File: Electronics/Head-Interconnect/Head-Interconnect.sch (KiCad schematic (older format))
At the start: 26 parts, among them J2 Conn_02x03_Odd_Even, J3 Conn_Coaxial, J4 Conn_01x04_MountingPin, J5 Conn_Coaxial, J6 Conn_01x04, J7 Conn_01x20_MountingPin

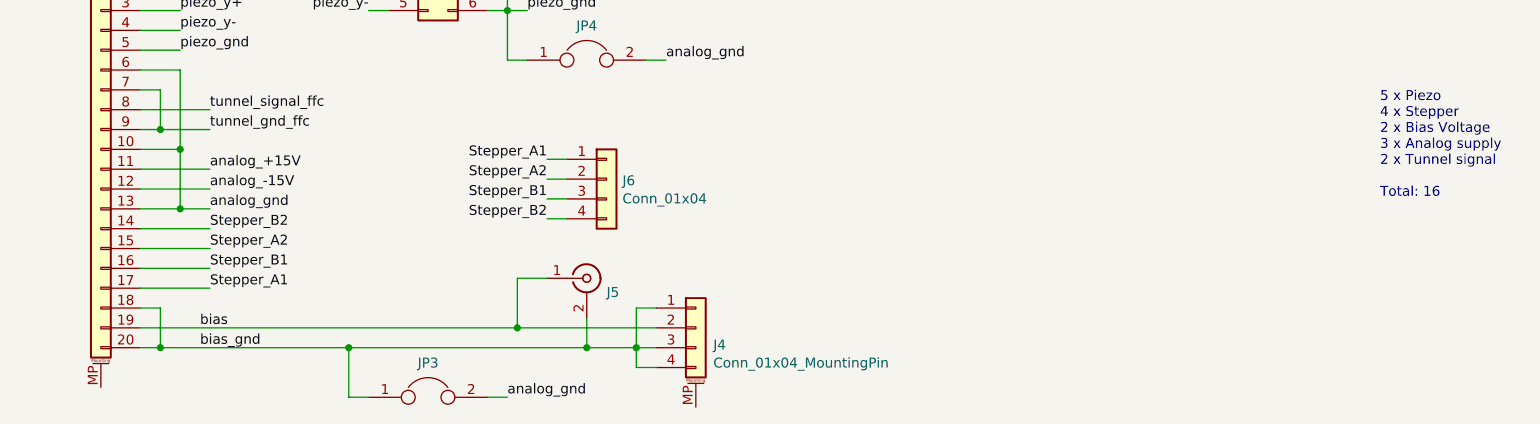
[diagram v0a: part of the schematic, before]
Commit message: Base interconnect and head interconnect in fabrication
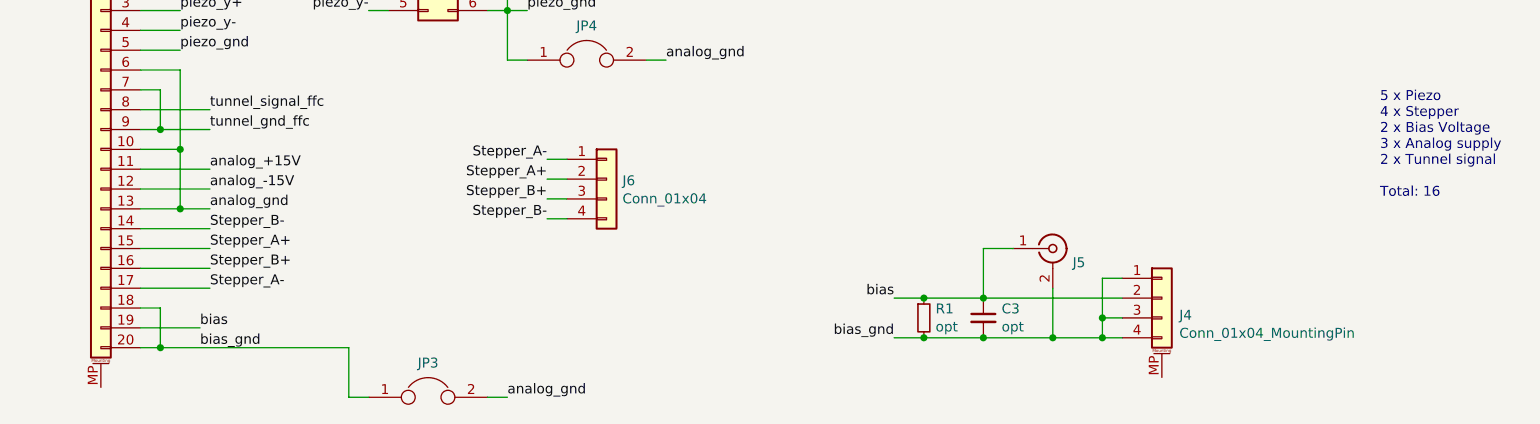
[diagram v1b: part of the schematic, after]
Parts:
- added C3: opt, Capacitor_SMD:C_0805_2012Metric_Pad1.15x1.40mm_HandSolder, symbol Device:C_Small
- added R1: opt, Resistor_SMD:R_0805_2012Metric_Pad1.15x1.40mm_HandSolder, symbol Device:R_Small
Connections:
- net bias: now also C3.1, R1.1
- net bias_gnd: now also C3.2, R1.2
- net Stepper_A1 renamed Stepper_A-
- net Stepper_A2 renamed Stepper_A+
- net Stepper_B1 renamed Stepper_B+
- net Stepper_B2 renamed Stepper_B-
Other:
- moved on the sheet: J4, J5
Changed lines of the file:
@@
 L Connector_Generic_MountingPin:Conn_01x04_MountingPin J4
 U 1 1 5F112DA2
-P 5700 6050
-F 0 "J4" H 5788 5964 50  0000 L CNN
-F 1 "Conn_01x04_MountingPin" H 5788 5873 50  0000 L CNN
-F 2 "Connector_FFC-FPC:TE_84953-4_1x04-1MP_P1.0mm_Horizontal" H 5700 6050 50  0001 C CNN
-F 3 "~" H 5700 6050 50  0001 C CNN
-	1    5700 6050
+P 8050 5900
+F 0 "J4" H 8138 5814 50  0000 L CNN
+F 1 "Conn_01x04_MountingPin" H 8138 5723 50  0000 L CNN
+F 2 "Connector_FFC-FPC:TE_84953-4_1x04-1MP_P1.0mm_Horizontal" H 8050 5900 50  0001 C CNN
+F 3 "~" H 8050 5900 50  0001 C CNN
+	1    8050 5900
 	1    0    0    -1
 $EndComp
@@
 L Connector:Conn_Coaxial J5
 U 1 1 5F12B036
-P 5150 5800
-F 0 "J5" H 5250 5729 50  0000 L CNN
-F 1 "Conn_Coaxial" H 5250 5684 50  0001 L CNN
-F 2 "Connector_Coaxial:MMCX_Molex_73415-1471_Vertical" H 5150 5800 50  0001 C CNN
-F 3 " ~" H 5150 5800 50  0001 C CNN
-	1    5150 5800
+P 7500 5650
+F 0 "J5" H 7600 5579 50  0000 L CNN
+F 1 "Conn_Coaxial" H 7600 5534 50  0001 L CNN
+F 2 "Connector_Coaxial:MMCX_Molex_73415-1471_Vertical" H 7500 5650 50  0001 C CNN
+F 3 " ~" H 7500 5650 50  0001 C CNN
+	1    7500 5650
 	1    0    0    -1
 $EndComp
@@
 Connection ~ 3000 6150
 Wire Wire Line
-	2900 6050 4800 6050
+	6700 5900 6850 5900
 Wire Wire Line
 	3000 6150 3950 6150
 Wire Wire Line
-	5500 5950 5400 5950
-Wire Wire Line
-	5400 5950 5400 6150
-Connection ~ 5400 6150
-Wire Wire Line
-	5400 6150 5500 6150
-Wire Wire Line
-	5400 6150 5400 6250
-Wire Wire Line
-	5400 6250 5500 6250
-Wire Wire Line
-	5150 6000 5150 6150
-Connection ~ 5150 6150
-Wire Wire Line
-	5150 6150 5400 6150
-Wire Wire Line
-	4950 5800 4800 5800
-Wire Wire Line
-	4800 5800 4800 6050
-Connection ~ 4800 6050
-Wire Wire Line
-	4800 6050 5500 6050
+	7850 5800 7750 5800
+Wire Wire Line
+	7750 5800 7750 6000
+Connection ~ 7750 6000
+Wire Wire Line
+	7750 6000 7850 6000
+Wire Wire Line
+	7750 6000 7750 6100
+Wire Wire Line
+	7750 6100 7850 6100
+Wire Wire Line
+	7500 5850 7500 6100
+Wire Wire Line
+	7300 5650 7150 5650
+Wire Wire Line
+	7150 5650 7150 5900
+Connection ~ 7150 5900
+Wire Wire Line
+	7150 5900 7850 5900
 Text Label 3200 6050 0    50   ~ 0
 bias
 Text Label 4950 5200 2    50   ~ 0
-Stepper_A1
+Stepper_A-
 Text Label 4950 5300 2    50   ~ 0
-Stepper_A2
+Stepper_A+
 Text Label 4950 5400 2    50   ~ 0
-Stepper_B1
+Stepper_B+
 Text Label 4950 5500 2    50   ~ 0
-Stepper_B2
+Stepper_B-
 Text Label 3250 5250 0    50   ~ 0
 analog_+15V
@@
 	4950 5500 5050 5500
 Text Label 3250 5850 0    50   ~ 0
-Stepper_A1
+Stepper_A-
 Text Label 3250 5650 0    50   ~ 0
-Stepper_A2
+Stepper_A+
 Text Label 3250 5750 0    50   ~ 0
-Stepper_B1
+Stepper_B+
 Text Label 3250 5550 0    50   ~ 0
-Stepper_B2
+Stepper_B-
 Wire Wire Line
 	3250 5550 2900 5550
@@
 Wire Wire Line
 	3950 6400 3950 6150
-Connection ~ 3950 6150
-Wire Wire Line
-	3950 6150 5150 6150
+Wire Wire Line
+	6700 6100 6850 6100
 $Comp
 L Device:Jumper JP4
@@
 	-1   0    0    -1
 $EndComp
+$Comp
+L Device:C_Small C3
+U 1 1 5F1041C2
+P 7150 6000
+F 0 "C3" H 7242 6046 50  0000 L CNN
+F 1 "opt" H 7242 5955 50  0000 L CNN
+F 2 "Capacitor_SMD:C_0805_2012Metric_Pad1.15x1.40mm_HandSolder" H 7150 6000 50  0001 C CNN
+F 3 "~" H 7150 6000 50  0001 C CNN
+	1    7150 6000
+	1    0    0    -1
+$EndComp
+$Comp
+L Device:R_Small R1
+U 1 1 5F1B34B3
+P 6850 6000
+F 0 "R1" H 6909 6046 50  0000 L CNN
+F 1 "opt" H 6909 5955 50  0000 L CNN
+F 2 "Resistor_SMD:R_0805_2012Metric_Pad1.15x1.40mm_HandSolder" H 6850 6000 50  0001 C CNN
+F 3 "~" H 6850 6000 50  0001 C CNN
+	1    6850 6000
+	1    0    0    -1
+$EndComp
+Wire Wire Line
+	2900 6050 3200 6050
+Text Label 6700 5900 2    50   ~ 0
+bias
+Text Label 6700 6100 2    50   ~ 0
+bias_gnd
+Wire Wire Line
+	7500 6100 7750 6100
+Connection ~ 7500 6100
+Connection ~ 7750 6100
+Connection ~ 7150 6100
+Wire Wire Line
+	7150 6100 7500 6100
+Connection ~ 6850 5900
+Wire Wire Line
+	6850 5900 7150 5900
+Connection ~ 6850 6100
+Wire Wire Line
+	6850 6100 7150 6100
 $EndSCHEMATC

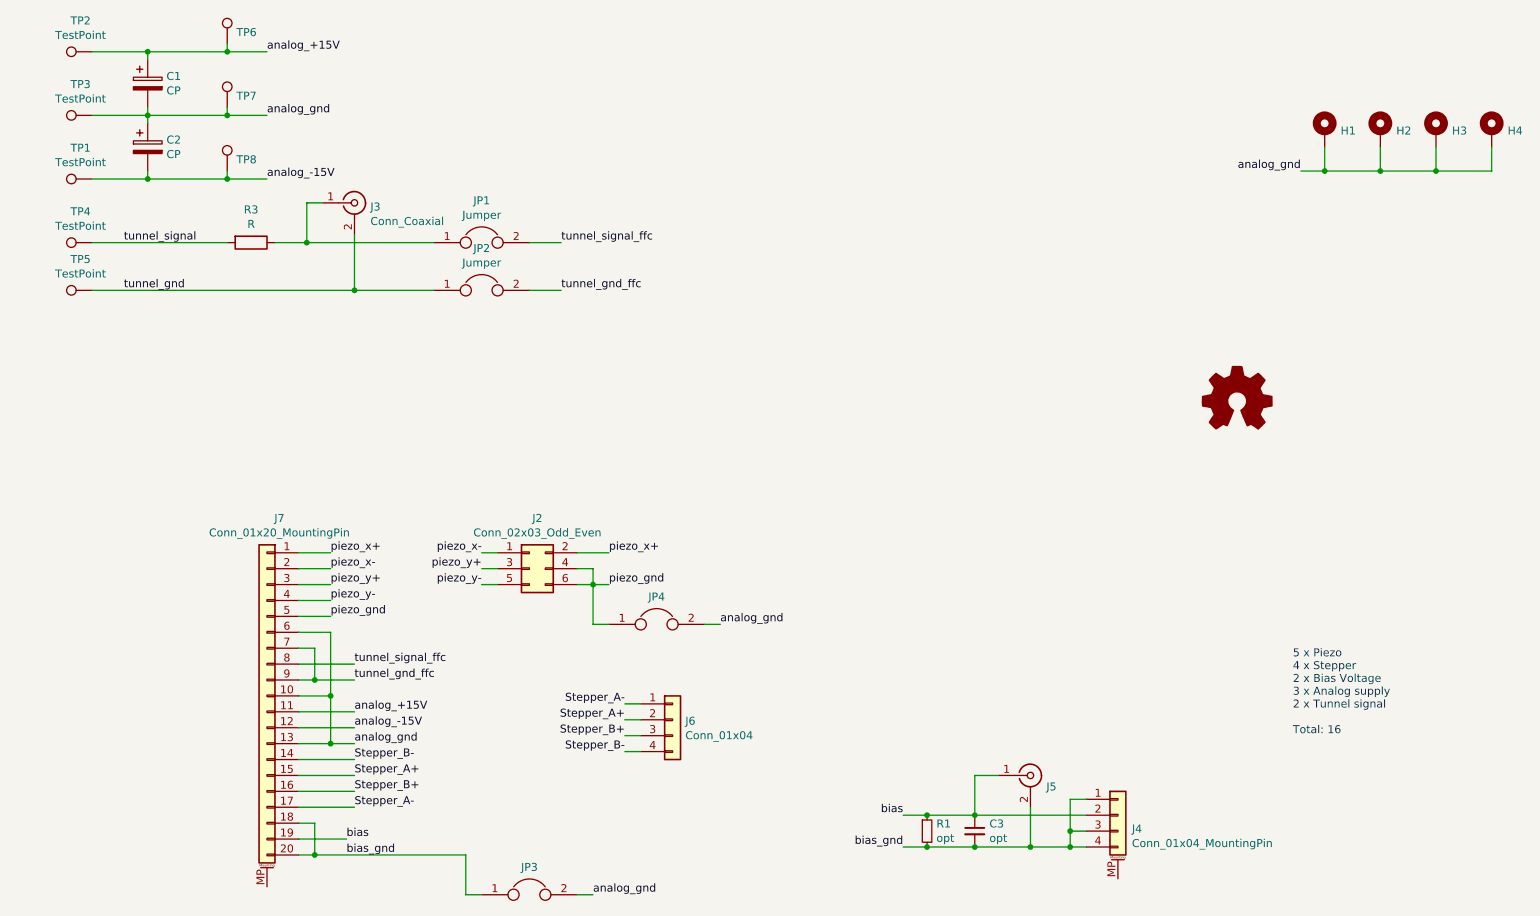
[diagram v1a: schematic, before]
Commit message: Added images
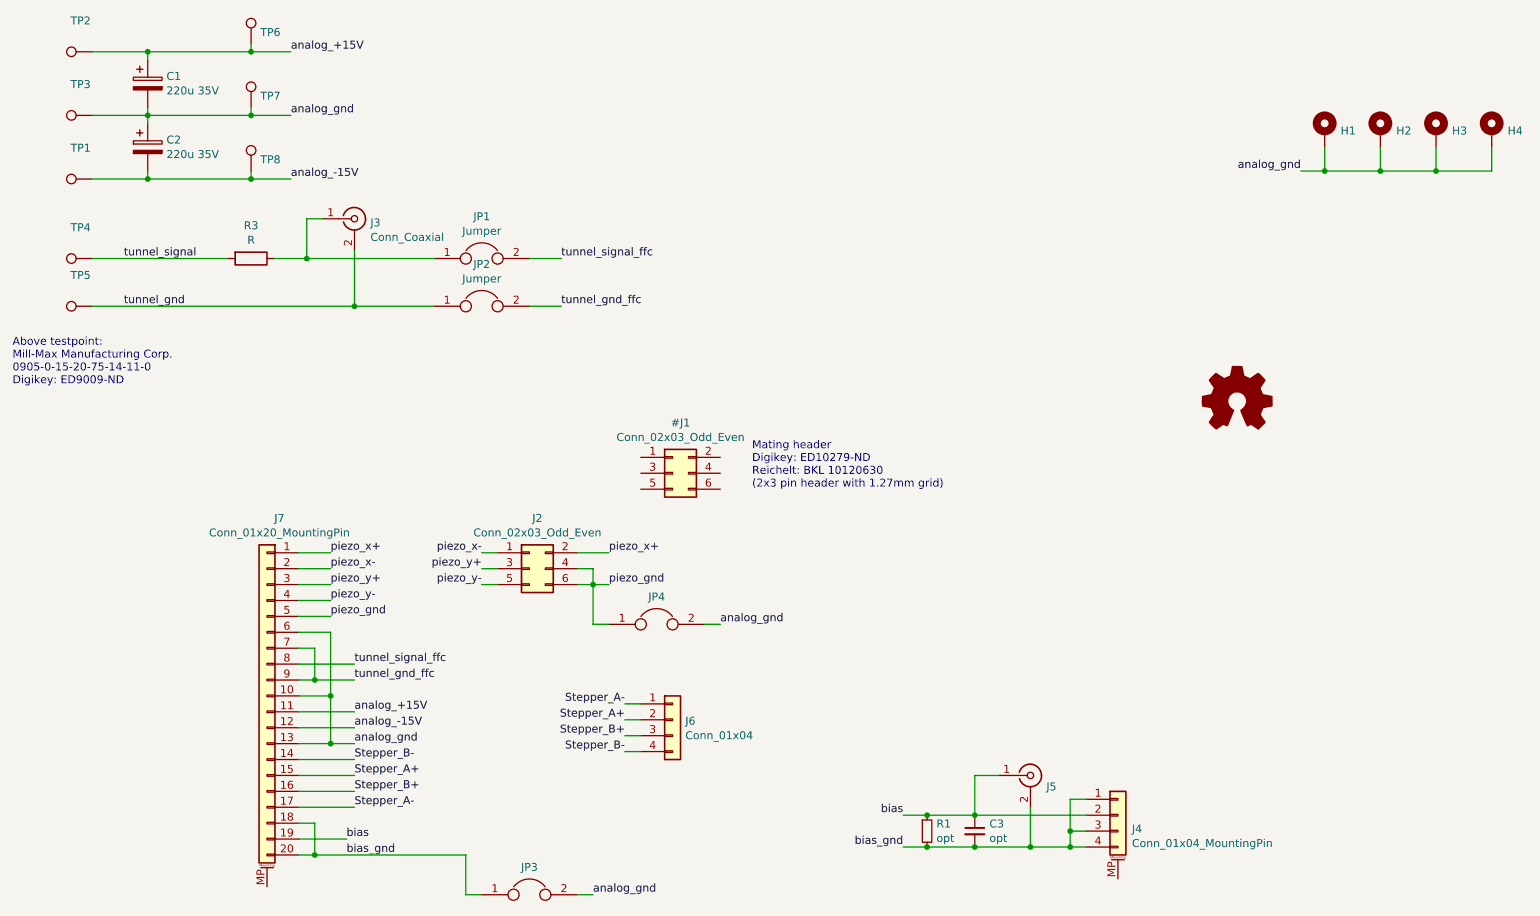
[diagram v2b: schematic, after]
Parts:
- C1, C2: value CP -> 220u 35V; Reichelt (none) -> VF 220/35 K-F
- J2: Digikey (none) -> 609-3704-1-ND
- J3, J5: Reichelt (none) -> R 110 426
- J4: Digikey (none) -> A33834CT-ND
- TP1, TP2, TP3, TP4, TP5: value TestPoint -> 0905-0-15-20-75-14-11-0; Digikey (none) -> ED9009-ND
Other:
- note added: "Mating header\nDigikey: ED10279-ND\nReichelt: BKL 10120630\n(2x3 pin header with 1.27mm grid)"
- note added: "\nAbove testpoint:\nMill-Max Manufacturing Corp.\n0905-0-15-20-75-14-11-0\nDigikey: ED9009-ND"
- note removed: "5 x Piezo\n4 x Stepper\n2 x Bias Voltage\n3 x Analog supply\n2 x Tunnel signal\n\nTotal: 16"
- moved on the sheet: J3, JP1, JP2, R3, TP4, TP5, TP6, TP7, TP8

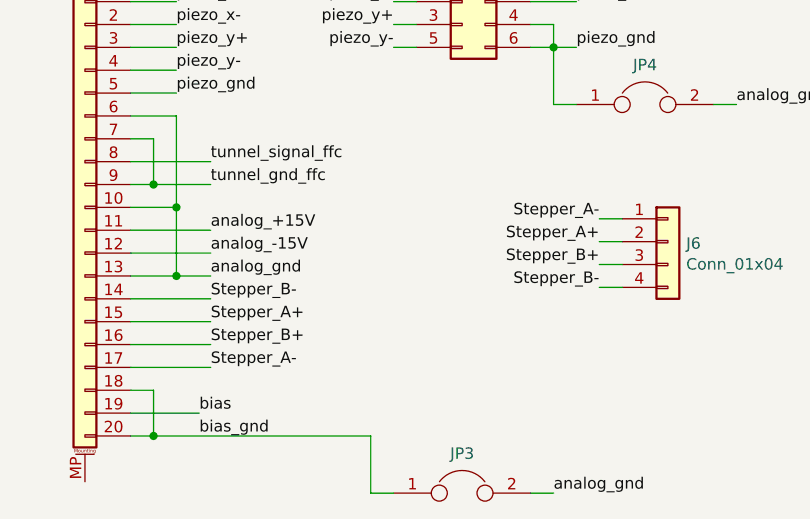
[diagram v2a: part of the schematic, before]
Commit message: Added sample-bias interconnect and base interconnect V2
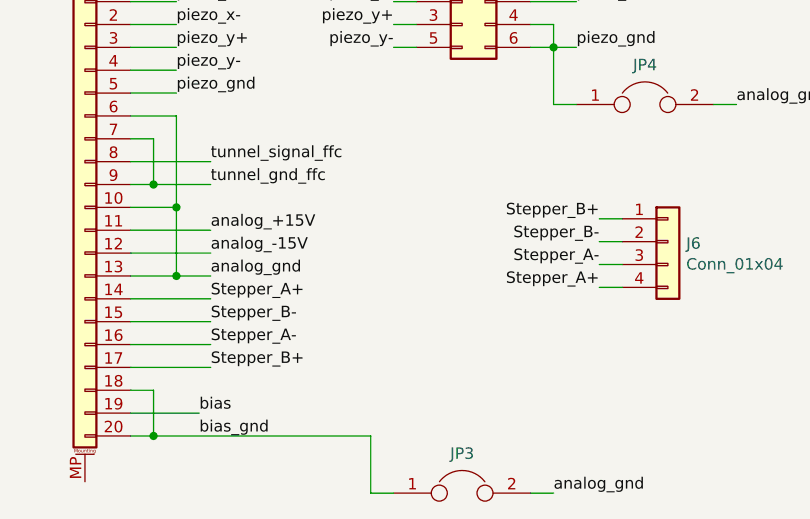
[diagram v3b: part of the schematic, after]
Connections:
- net Stepper_A+: now also J6.4 (Pin_4), J7.14 (Pin_14); no longer J6.2 (Pin_2), J7.15 (Pin_15)
- net Stepper_A-: now also J6.3 (Pin_3), J7.16 (Pin_16); no longer J6.1 (Pin_1), J7.17 (Pin_17)
- net Stepper_B+: now also J6.1 (Pin_1), J7.17 (Pin_17); no longer J6.3 (Pin_3), J7.16 (Pin_16)
- net Stepper_B-: now also J6.2 (Pin_2), J7.15 (Pin_15); no longer J6.4 (Pin_4), J7.14 (Pin_14)
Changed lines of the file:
@@
 Text Label 3200 6050 0    50   ~ 0
 bias
+Text Label 4950 5400 2    50   ~ 0
+Stepper_A-
+Text Label 4950 5500 2    50   ~ 0
+Stepper_A+
 Text Label 4950 5200 2    50   ~ 0
-Stepper_A-
+Stepper_B+
 Text Label 4950 5300 2    50   ~ 0
-Stepper_A+
-Text Label 4950 5400 2    50   ~ 0
-Stepper_B+
-Text Label 4950 5500 2    50   ~ 0
 Stepper_B-
 Text Label 3250 5250 0    50   ~ 0
@@
 Wire Wire Line
 	4950 5500 5050 5500
+Text Label 3250 5750 0    50   ~ 0
+Stepper_A-
+Text Label 3250 5550 0    50   ~ 0
+Stepper_A+
 Text Label 3250 5850 0    50   ~ 0
-Stepper_A-
+Stepper_B+
 Text Label 3250 5650 0    50   ~ 0
-Stepper_A+
-Text Label 3250 5750 0    50   ~ 0
-Stepper_B+
-Text Label 3250 5550 0    50   ~ 0
 Stepper_B-
 Wire Wire Line

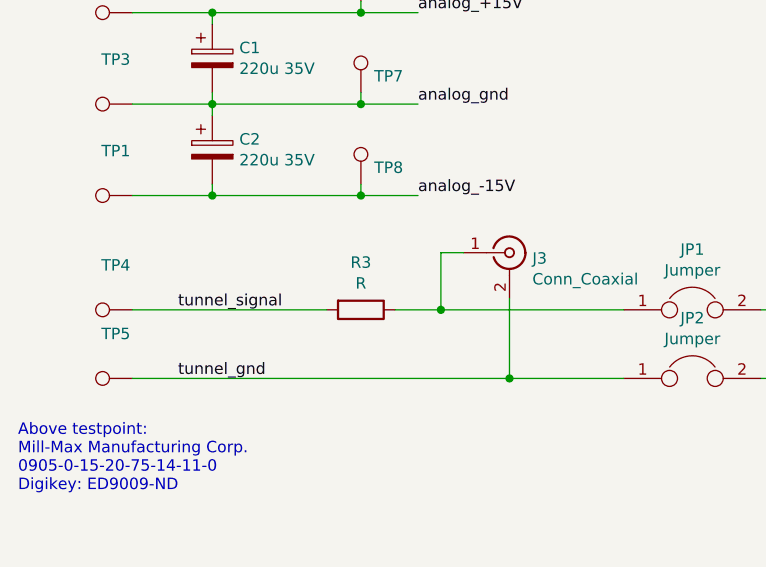
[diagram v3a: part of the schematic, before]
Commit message: Added value to R3 on head interconnect
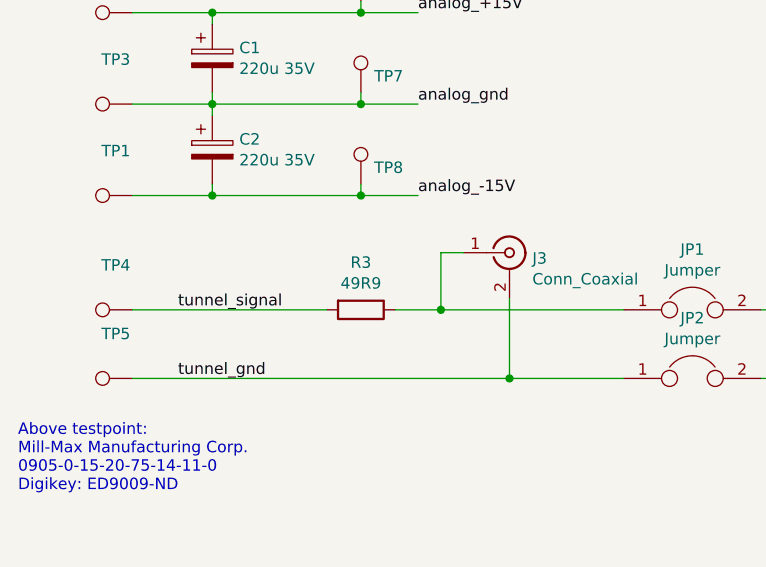
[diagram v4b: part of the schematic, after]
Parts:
- R3: value R -> 49R9
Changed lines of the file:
@@
 P 2600 2400
 F 0 "R3" V 2393 2400 50  0000 C CNN
-F 1 "R" V 2484 2400 50  0000 C CNN
+F 1 "49R9" V 2484 2400 50  0000 C CNN
 F 2 "Resistor_SMD:R_0805_2012Metric_Pad1.15x1.40mm_HandSolder" V 2530 2400 50  0001 C CNN
 F 3 "~" H 2600 2400 50  0001 C CNN
